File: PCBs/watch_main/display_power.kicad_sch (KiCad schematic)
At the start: 3 parts, among them IC1401 TPS65631WDSKR

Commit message: Created firmware project
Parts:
- renumbered C1402 to C1401, C1401 to C1402
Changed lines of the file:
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@@
   (symbol (lib_id "watch_symbols_lib:+VSYS") (at 121.92 81.28 0) (unit 1)
     (in_bom yes) (on_board yes) (dnp no) (fields_autoplaced)
-    (property "Reference" "#PWR01402" (at 121.92 85.09 0)
+    (property "Reference" "#PWR01401" (at 121.92 85.09 0)
       (effects (font (size 1.27 1.27)) hide)
     )
@@
       (project "watch_main"
         (path "/b008648a-c7cf-4e14-8a0a-b9314d757b4a/2c0a5010-ab28-463f-b516-9128de6cd18d"
-          (reference "#PWR01402") (unit 1)
+          (reference "#PWR01401") (unit 1)
         )
       )
@@
   (symbol (lib_id "Device:C_Small") (at 134.62 91.44 0) (unit 1)
     (in_bom yes) (on_board yes) (dnp no)
-    (property "Reference" "C1401" (at 132.08 90.1763 0)
+    (property "Reference" "C1402" (at 132.08 90.1763 0)
       (effects (font (size 1.27 1.27)) (justify right))
     )
@@
       (project "watch_main"
         (path "/b008648a-c7cf-4e14-8a0a-b9314d757b4a/2c0a5010-ab28-463f-b516-9128de6cd18d"
-          (reference "C1401") (unit 1)
+          (reference "C1402") (unit 1)
         )
       )
@@
   (symbol (lib_id "Device:C_Small") (at 121.92 91.44 0) (unit 1)
     (in_bom yes) (on_board yes) (dnp no)
-    (property "Reference" "C1402" (at 119.38 90.1763 0)
+    (property "Reference" "C1401" (at 119.38 90.1763 0)
       (effects (font (size 1.27 1.27)) (justify right))
     )
@@
       (project "watch_main"
         (path "/b008648a-c7cf-4e14-8a0a-b9314d757b4a/2c0a5010-ab28-463f-b516-9128de6cd18d"
-          (reference "C1402") (unit 1)
+          (reference "C1401") (unit 1)
         )
       )
@@
   (symbol (lib_id "power:GND") (at 134.62 104.14 0) (unit 1)
     (in_bom yes) (on_board yes) (dnp no) (fields_autoplaced)
-    (property "Reference" "#PWR01401" (at 134.62 110.49 0)
+    (property "Reference" "#PWR01403" (at 134.62 110.49 0)
       (effects (font (size 1.27 1.27)) hide)
     )
@@
       (project "watch_main"
         (path "/b008648a-c7cf-4e14-8a0a-b9314d757b4a/2c0a5010-ab28-463f-b516-9128de6cd18d"
-          (reference "#PWR01401") (unit 1)
+          (reference "#PWR01403") (unit 1)
         )
       )
@@
   (symbol (lib_id "power:GND") (at 121.92 96.52 0) (unit 1)
     (in_bom yes) (on_board yes) (dnp no) (fields_autoplaced)
-    (property "Reference" "#PWR01403" (at 121.92 102.87 0)
+    (property "Reference" "#PWR01402" (at 121.92 102.87 0)
       (effects (font (size 1.27 1.27)) hide)
     )
@@
       (project "watch_main"
         (path "/b008648a-c7cf-4e14-8a0a-b9314d757b4a/2c0a5010-ab28-463f-b516-9128de6cd18d"
-          (reference "#PWR01403") (unit 1)
+          (reference "#PWR01402") (unit 1)
         )
       )

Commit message: Progress with schematic and RFID simulations
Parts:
- added C1403, C1404: 10u, Capacitor_SMD:C_0402_1005Metric, symbol Device:C_Small
- added L1401, L1402: 10u, Inductor_SMD:L_0805_2012Metric, symbol Device:L_Small
- C1401: value 100nF -> 10u
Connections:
- net +4V6: now also IC1401.4 (FBS), C1403.1
- net +VSYS: now also L1402.1
- net -2V2: now also C1404.1
- net GND: now also C1403.2, C1404.2, L1401.2
- net SWP: now reaches IC1401.1 (SWP)
- net SWP: now also L1402.2
- net SWN: now reaches IC1401.8 (SWN)
- net SWN: now also L1401.1

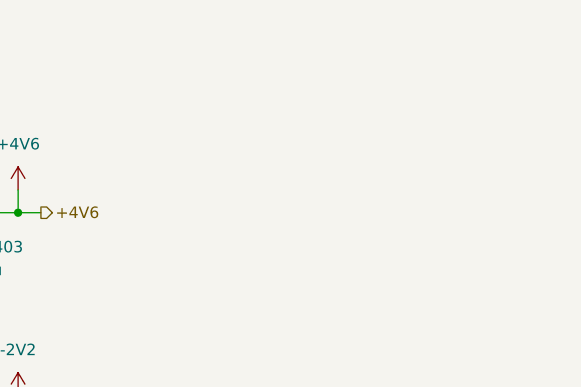
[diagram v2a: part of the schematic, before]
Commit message: Schematic finished and BOM started
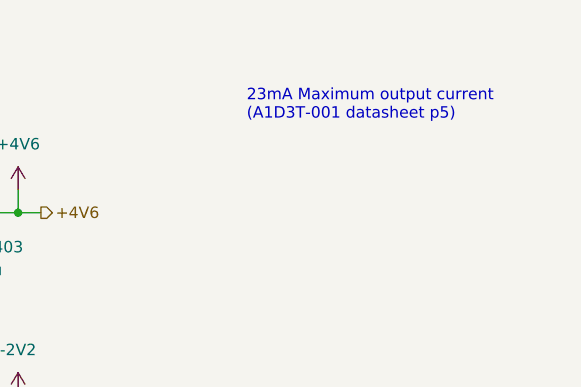
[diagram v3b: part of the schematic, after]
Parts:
- L1401, L1402: footprint Inductor_SMD:L_0805_2012Metric -> Inductor_SMD:L_TDK_MLZ1608
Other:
- note added: "23mA Maximum output current (A1D3T-001 datasheet p5)"
- title: (none) -> Watch Display Power
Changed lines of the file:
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@@
 (kicad_sch (version 20230121) (generator eeschema)
   (paper "A4")
+  (title_block
+    (title "Watch Display Power")
+    (date "2023-12-21")
+    (rev "1")
+    (comment 1 "Checked by Ben Smith 21/12/23")
+  )
   (junction (at 134.62 99.06) (diameter 0) (color 0 0 0 0)
   )
@@
   (wire (pts (xy 134.62 101.6) (xy 134.62 99.06))
     (stroke (width 0) (type default))
+  )
+  (text "23mA Maximum output current\n(A1D3T-001 datasheet p5)"
+    (at 215.9 76.2 0)
+    (effects (font (size 1.27 1.27)) (justify left bottom))
   )
   (label "SWP" (at 167.64 83.82 0) (fields_autoplaced)
@@
       (effects (font (size 1.27 1.27)))
     )
-    (property "Footprint" "Inductor_SMD:L_0805_2012Metric" (at 152.4 71.12 0)
+    (property "Footprint" "Inductor_SMD:L_TDK_MLZ1608" (at 152.4 71.12 0)
       (effects (font (size 1.27 1.27)) hide)
     )
@@
       (effects (font (size 1.27 1.27)) (justify left))
     )
-    (property "Footprint" "Inductor_SMD:L_0805_2012Metric" (at 170.18 116.84 0)
-      (effects (font (size 1.27 1.27)) hide)
-    )
+    (property "Footprint" "Inductor_SMD:L_TDK_MLZ1608" (at 170.18 116.84 0)
+      (effects (font (size 1.27 1.27)) hide)
+    )

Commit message: Started routing main PCB
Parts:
- renumbered L1402 to L1401, L1401 to L1402
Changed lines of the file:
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@@
   (symbol (lib_id "Device:L_Small") (at 152.4 71.12 90) (unit 1)
     (in_bom yes) (on_board yes) (dnp no)
-    (property "Reference" "L1402" (at 152.4 66.04 90)
+    (property "Reference" "L1401" (at 152.4 66.04 90)
       (effects (font (size 1.27 1.27)))
     )
@@
       (project "watch_main"
         (path "/b008648a-c7cf-4e14-8a0a-b9314d757b4a/2c0a5010-ab28-463f-b516-9128de6cd18d"
-          (reference "L1402") (unit 1)
+          (reference "L1401") (unit 1)
         )
       )
@@
   (symbol (lib_id "power:GND") (at 182.88 119.38 0) (unit 1)
     (in_bom yes) (on_board yes) (dnp no) (fields_autoplaced)
-    (property "Reference" "#PWR01407" (at 182.88 125.73 0)
+    (property "Reference" "#PWR01406" (at 182.88 125.73 0)
       (effects (font (size 1.27 1.27)) hide)
     )
@@
       (project "watch_main"
         (path "/b008648a-c7cf-4e14-8a0a-b9314d757b4a/2c0a5010-ab28-463f-b516-9128de6cd18d"
-          (reference "#PWR01407") (unit 1)
+          (reference "#PWR01406") (unit 1)
         )
         (path "/b008648a-c7cf-4e14-8a0a-b9314d757b4a/a7679e4f-f097-4da0-abbe-b751bbcda887"
@@
   (symbol (lib_id "Device:L_Small") (at 170.18 116.84 0) (unit 1)
     (in_bom yes) (on_board yes) (dnp no) (fields_autoplaced)
-    (property "Reference" "L1401" (at 171.45 116.205 0)
+    (property "Reference" "L1402" (at 171.45 116.205 0)
       (effects (font (size 1.27 1.27)) (justify left))
     )
@@
       (project "watch_main"
         (path "/b008648a-c7cf-4e14-8a0a-b9314d757b4a/2c0a5010-ab28-463f-b516-9128de6cd18d"
-          (reference "L1401") (unit 1)
+          (reference "L1402") (unit 1)
         )
       )
@@
   (symbol (lib_id "power:GND") (at 182.88 96.52 0) (unit 1)
     (in_bom yes) (on_board yes) (dnp no) (fields_autoplaced)
-    (property "Reference" "#PWR01408" (at 182.88 102.87 0)
+    (property "Reference" "#PWR01405" (at 182.88 102.87 0)
       (effects (font (size 1.27 1.27)) hide)
     )
@@
       (project "watch_main"
         (path "/b008648a-c7cf-4e14-8a0a-b9314d757b4a/2c0a5010-ab28-463f-b516-9128de6cd18d"
-          (reference "#PWR01408") (unit 1)
+          (reference "#PWR01405") (unit 1)
         )
         (path "/b008648a-c7cf-4e14-8a0a-b9314d757b4a/a7679e4f-f097-4da0-abbe-b751bbcda887"
@@
   (symbol (lib_id "power:GND") (at 170.18 121.92 0) (unit 1)
     (in_bom yes) (on_board yes) (dnp no) (fields_autoplaced)
-    (property "Reference" "#PWR01406" (at 170.18 128.27 0)
+    (property "Reference" "#PWR01404" (at 170.18 128.27 0)
       (effects (font (size 1.27 1.27)) hide)
     )
@@
       (project "watch_main"
         (path "/b008648a-c7cf-4e14-8a0a-b9314d757b4a/2c0a5010-ab28-463f-b516-9128de6cd18d"
-          (reference "#PWR01406") (unit 1)
+          (reference "#PWR01404") (unit 1)
         )
         (path "/b008648a-c7cf-4e14-8a0a-b9314d757b4a/a7679e4f-f097-4da0-abbe-b751bbcda887"
@@
   (symbol (lib_id "watch_symbols_lib:+4V6") (at 190.5 83.82 0) (unit 1)
     (in_bom yes) (on_board yes) (dnp no) (fields_autoplaced)
-    (property "Reference" "#PWR01404" (at 190.5 87.63 0)
+    (property "Reference" "#PWR01407" (at 190.5 87.63 0)
       (effects (font (size 1.27 1.27)) hide)
     )
@@
       (project "watch_main"
         (path "/b008648a-c7cf-4e14-8a0a-b9314d757b4a/2c0a5010-ab28-463f-b516-9128de6cd18d"
-          (reference "#PWR01404") (unit 1)
+          (reference "#PWR01407") (unit 1)
         )
         (path "/b008648a-c7cf-4e14-8a0a-b9314d757b4a/a7679e4f-f097-4da0-abbe-b751bbcda887"
@@
   (symbol (lib_id "watch_symbols_lib:-2V2") (at 190.5 106.68 0) (unit 1)
     (in_bom yes) (on_board yes) (dnp no) (fields_autoplaced)
-    (property "Reference" "#PWR01405" (at 190.5 110.49 0)
+    (property "Reference" "#PWR01408" (at 190.5 110.49 0)
       (effects (font (size 1.27 1.27)) hide)
     )
@@
       (project "watch_main"
         (path "/b008648a-c7cf-4e14-8a0a-b9314d757b4a/2c0a5010-ab28-463f-b516-9128de6cd18d"
-          (reference "#PWR01405") (unit 1)
-        )
-        (path "/b008648a-c7cf-4e14-8a0a-b9314d757b4a/a7679e4f-f097-4da0-abbe-b751bbcda887"
+          (reference "#PWR01408") (unit 1)
+        )
+        (path "/b008648a-c7cf-4e14-8a0a-b9314d757b4a/a7679e4f-f097-4da0-abbe-b751bbcda887"
